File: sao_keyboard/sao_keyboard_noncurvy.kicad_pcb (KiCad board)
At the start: 2 copper layers, 96 x 33 mm, 59 parts, among them J4 I2C, J5 I2C, J6 sao_v2_addon_tht, U1 74LS245, U2 74LS245, U3 74LS245, U4 74LS245, U5 74LS245, U6 CH32V003F4P6, U7 24LC00

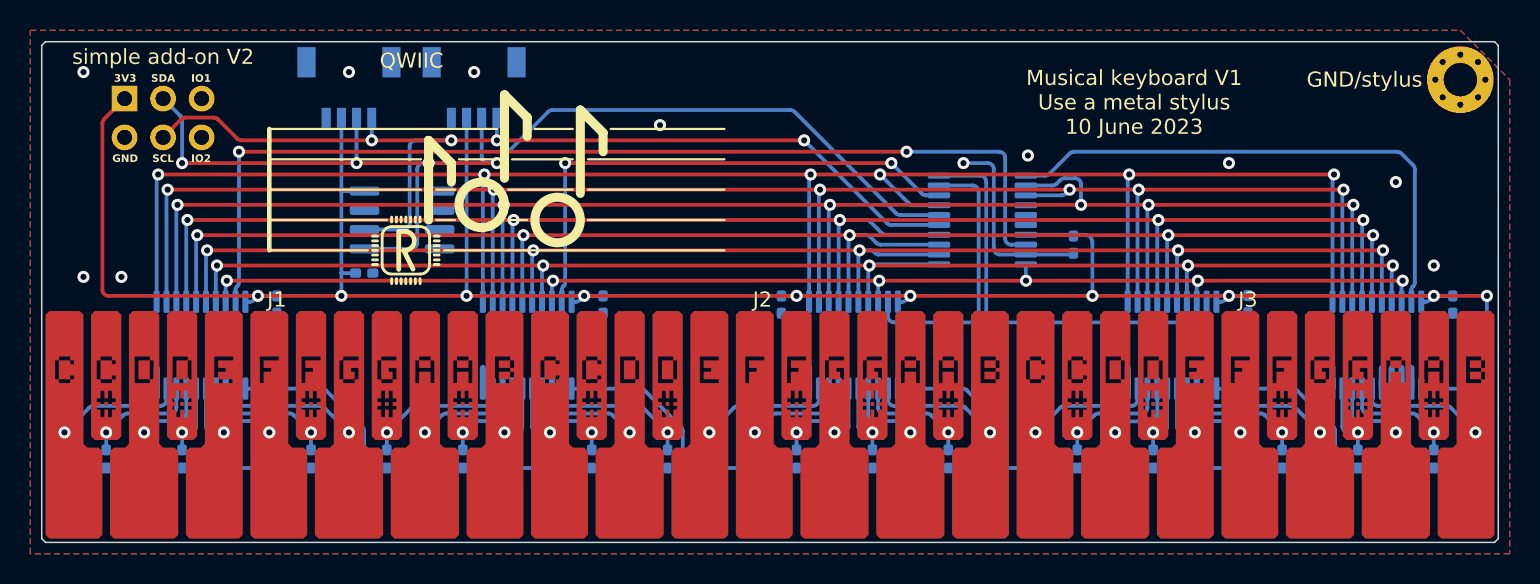
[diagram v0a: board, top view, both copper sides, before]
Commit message: Curvify the keyboard
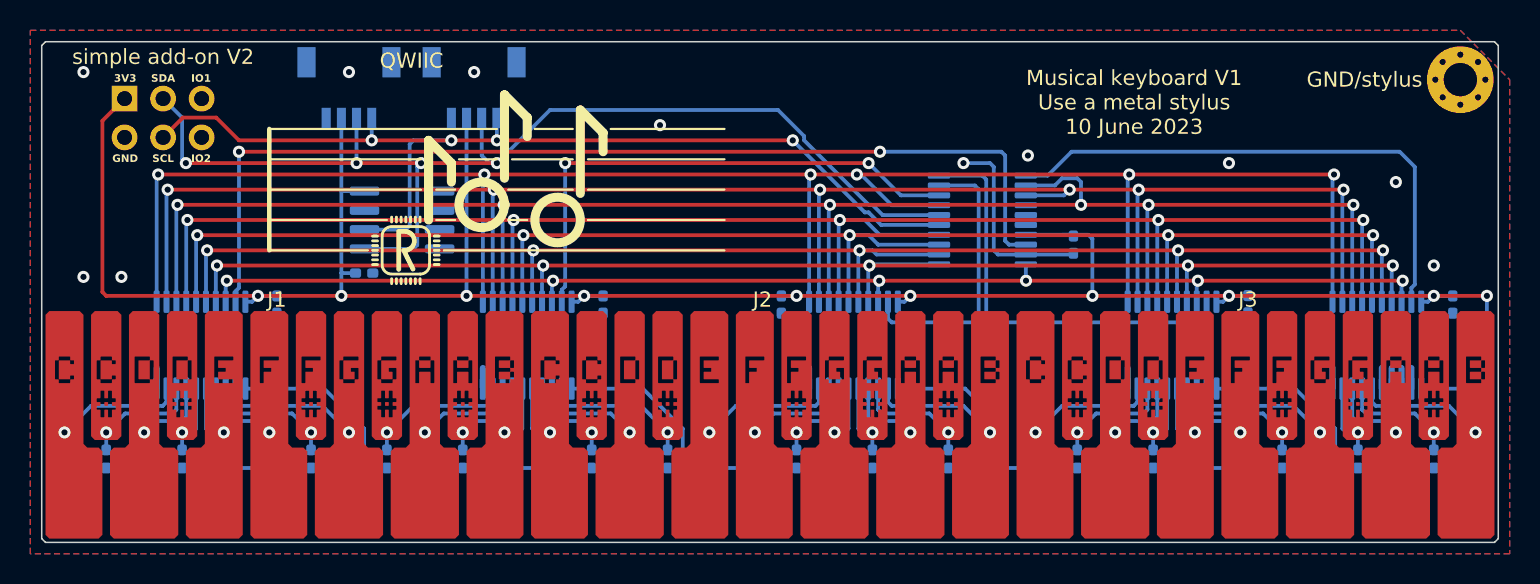
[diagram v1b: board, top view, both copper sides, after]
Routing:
- net Y0: track 124.4 -> 125.9 mm
